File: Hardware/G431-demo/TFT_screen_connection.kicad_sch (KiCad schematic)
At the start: 1 part, among them J7 Conn_01x18_MountingPin

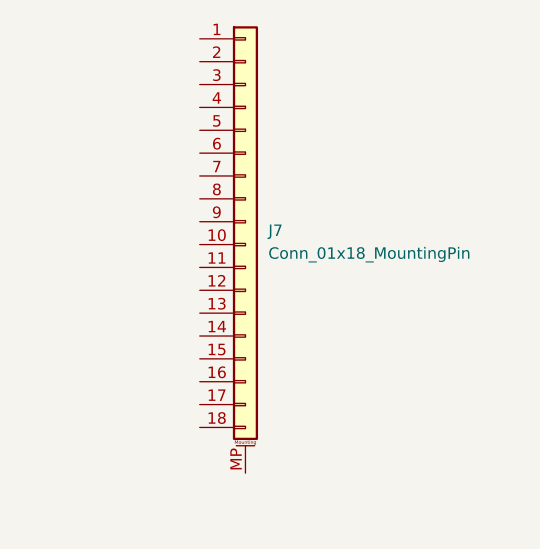
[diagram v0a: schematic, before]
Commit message: Schemetic done; PCB component layout
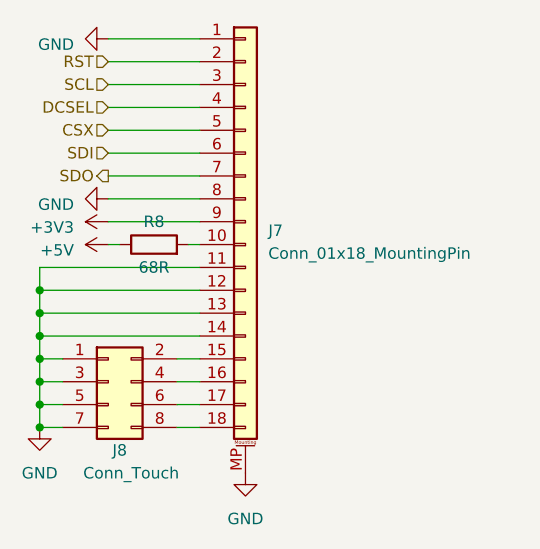
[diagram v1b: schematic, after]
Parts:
- added J8: Conn_Touch, Connector_PinSocket_2.54mm:PinSocket_2x04_P2.54mm_Vertical, symbol Connector_Generic:Conn_02x04_Odd_Even
- added R8: 68R, Resistor_SMD:R_1812_4532Metric, symbol Device:R
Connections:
- net GND: now reaches J7.1 (Pin_1)
- net GND: now also J7.11 (Pin_11), J7.12 (Pin_12), J7.13 (Pin_13), J7.14 (Pin_14), J7.8 (Pin_8), J7.MP (MountPin), J8.1 (Pin_1), J8.3 (Pin_3), J8.5 (Pin_5), J8.7 (Pin_7)
- net at J7.10 (Pin_10): now also R8.2
- net at J7.15 (Pin_15): now also J8.2 (Pin_2)
- net at J7.16 (Pin_16): now also J8.4 (Pin_4)
- net at J7.17 (Pin_17): now also J8.6 (Pin_6)
- net at J7.18 (Pin_18): now also J8.8 (Pin_8)
- net RST: now reaches J7.2 (Pin_2)
- net SCL: now reaches J7.3 (Pin_3)
- net DCSEL: now reaches J7.4 (Pin_4)
- net CSX: now reaches J7.5 (Pin_5)
- net SDI: now reaches J7.6 (Pin_6)
- net SDO: now reaches J7.7 (Pin_7)
- net +3V3: now reaches J7.9 (Pin_9)
- new net +5V: R8.1
